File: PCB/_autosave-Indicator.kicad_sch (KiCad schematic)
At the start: 6 parts

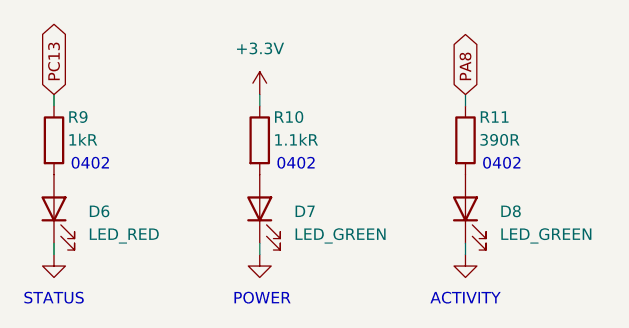
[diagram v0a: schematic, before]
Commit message: Minor Schematic tweaks like - Adding pull up resistors to the spare GPIO pins - Renaming some Global Labels - Labeling all the pins on the STM32 correctly
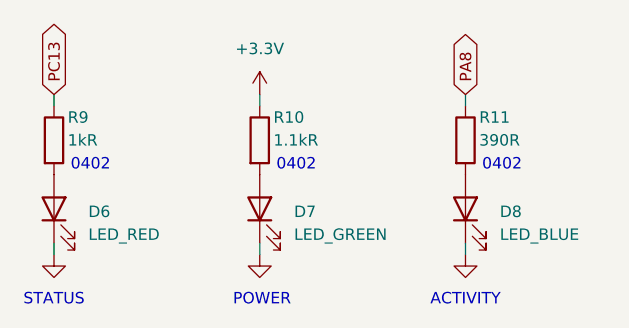
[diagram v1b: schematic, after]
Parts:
- D8: value LED_GREEN -> LED_BLUE
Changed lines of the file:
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@@
 			)
 		)
-		(property "Value" "LED_GREEN"
+		(property "Value" "LED_BLUE"
 			(at 77.47 42.2274 90)
 			(show_name no)
